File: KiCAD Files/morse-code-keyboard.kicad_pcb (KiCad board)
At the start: 2 copper layers, 35 parts, among them IC1 AZ1117IH-3.3TRG1, IC2 USBLC6-2SC6, J1 UJ32-C-H-G-H2-SMT-TR, J3 61300511121, SW1 SW_Push, SW2 SW_Push, SW3 SW_Push, SW4 SW_Push, SW8 SW_Push, SW9 SW_Push, U2 STM32H7A3VGTx, Y1 LFXTAL010595

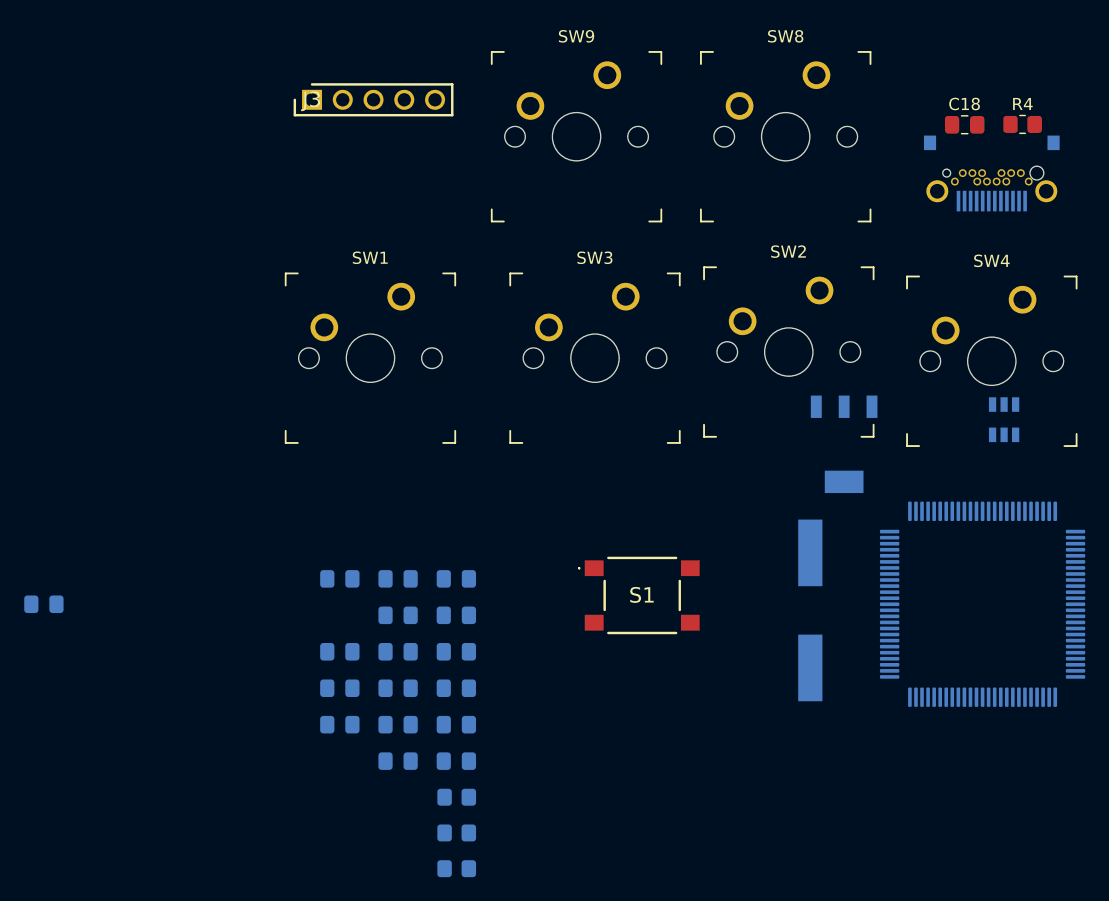
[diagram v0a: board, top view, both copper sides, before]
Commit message: changed out microcontroller
Might add in a bit of debug circuitry + button leds will see tmmrw
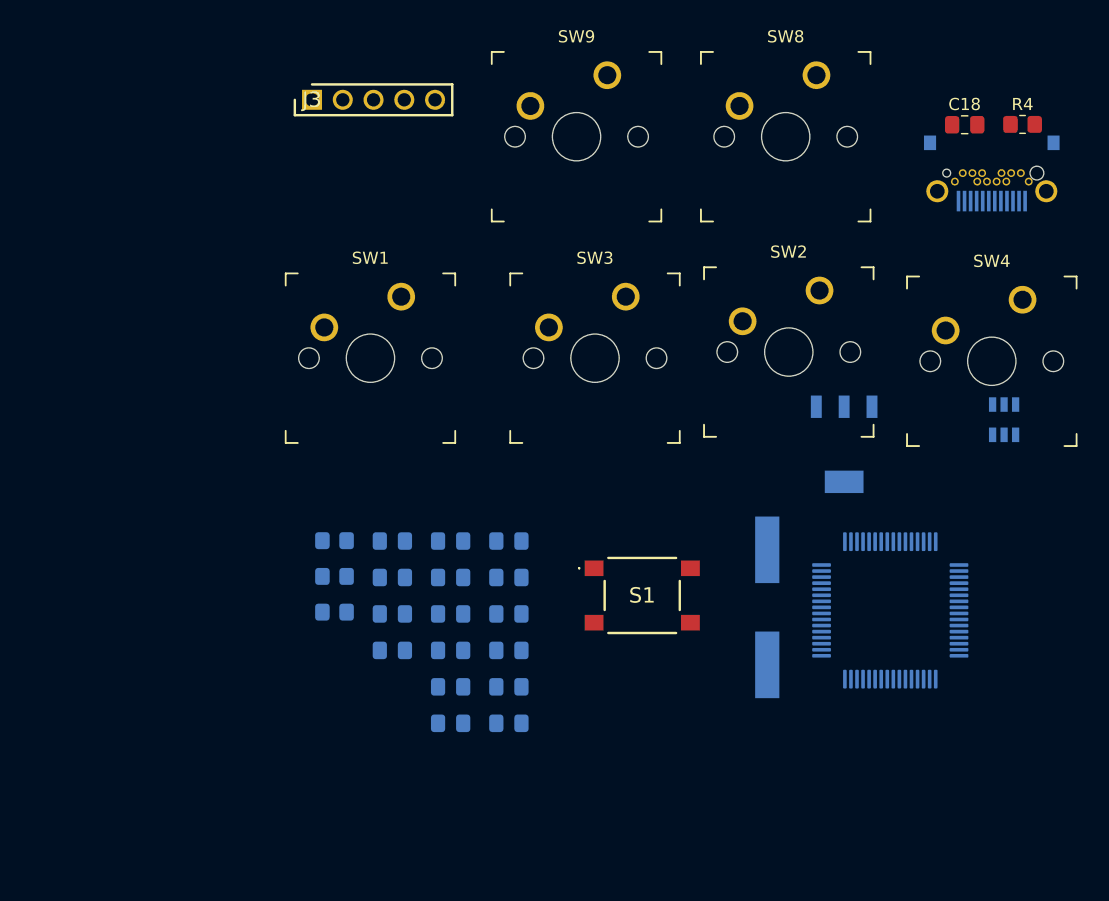
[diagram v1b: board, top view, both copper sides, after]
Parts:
- removed C8: 100n, Capacitor_SMD:C_0805_2012Metric_Pad1.18x1.45mm_HandSolder
- removed U2: STM32H7A3VGTx, Package_QFP:LQFP-100_14x14mm_P0.5mm
- added U1: STM32H7A3RGTx, Package_QFP:LQFP-64_10x10mm_P0.5mm, B.Cu at (110.5, 102.9)
- moved C14 29.2 mm to (69.4, 97.1)
- moved R1 23.5 mm to (64.6, 97.1)
- moved R2 23.5 mm to (64.6, 100.1)
- moved R3 23.5 mm to (64.6, 103.0)
- moved C13 15.0 mm to (74.2, 112.2)
- moved C10 7.51 mm to (74.2, 103.2)
- moved C11 7.51 mm to (74.2, 106.2)
- moved C12 7.51 mm to (74.2, 109.2)
- moved C15 7.51 mm to (69.4, 100.2)
- moved C16 7.51 mm to (69.4, 103.2)
- moved C17 7.51 mm to (69.4, 106.2)
- moved C9 7.51 mm to (74.2, 100.2)
- moved C1 5.35 mm to (79.0, 97.1)
- moved C4 5.35 mm to (79.0, 106.2)
- moved C6 5.35 mm to (79.0, 112.2)
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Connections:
- IC2 pad 1: D+ -> D-
- IC2 pad 3: D- -> D+
- IC2 pad 4: USB- -> USB+
- IC2 pad 6: USB+ -> USB-
